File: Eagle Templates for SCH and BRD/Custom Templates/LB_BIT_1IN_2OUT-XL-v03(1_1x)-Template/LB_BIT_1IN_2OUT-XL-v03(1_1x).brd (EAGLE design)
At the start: 21.6 x 38 mm, 21 parts, among them U1 LV321SOT23-5, U2 LV321SOT23-5, U3 LV321SOT23-5

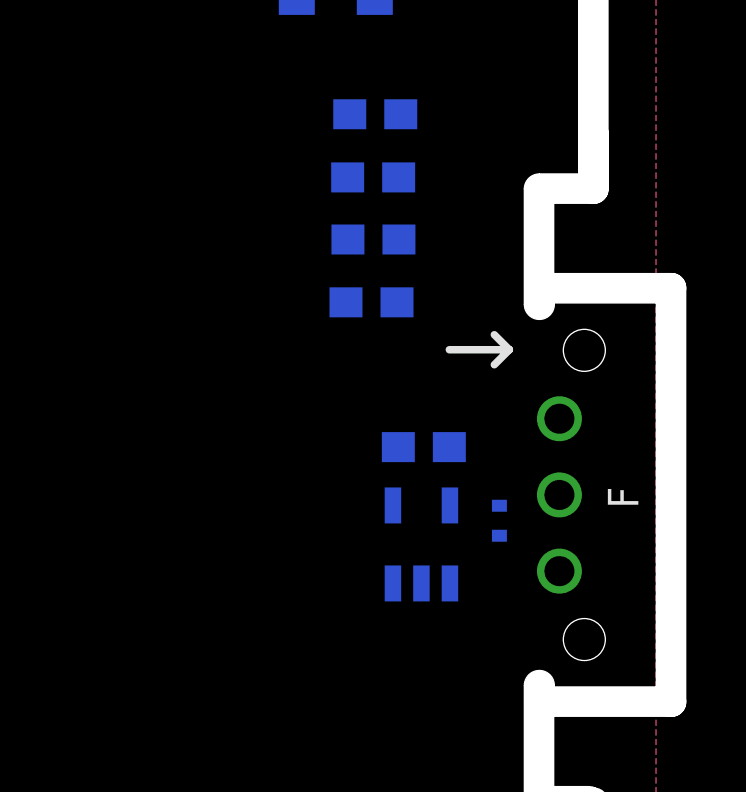
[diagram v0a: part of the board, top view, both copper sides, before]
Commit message: added bitlab logo and made minor changes to board templates. Updated littlebits library.
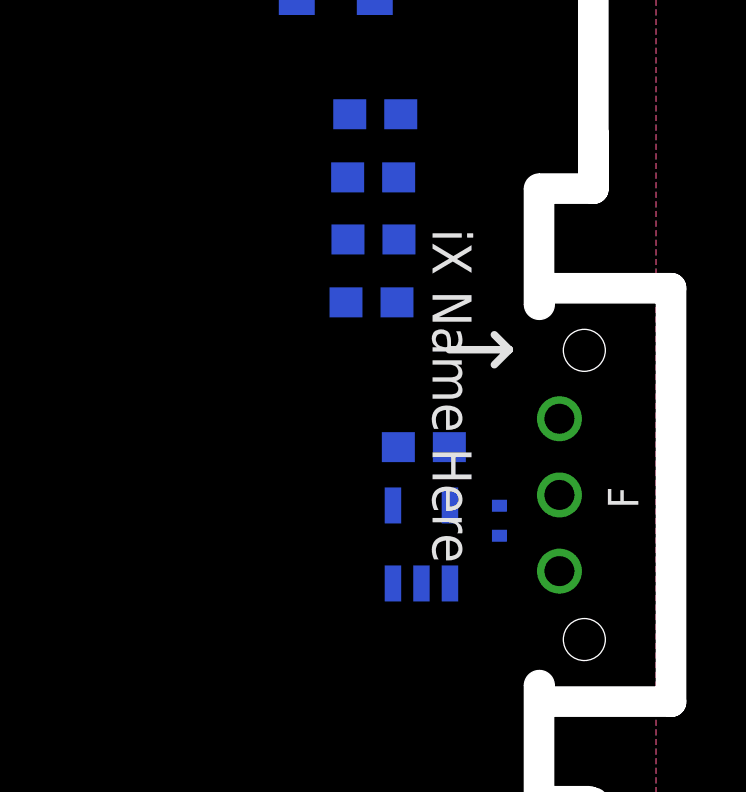
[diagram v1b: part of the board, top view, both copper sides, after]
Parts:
- added U$3: (no value), LITTLEBITS:BITLAB-LOGO
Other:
- board text added: "iX Name Here"
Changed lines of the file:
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@@
 <layer number="113" name="extra" color="10" fill="1" visible="yes" active="yes"/>
 <layer number="116" name="Patch_BOT" color="9" fill="4" visible="yes" active="yes"/>
+<layer number="118" name="Rect_Pads" color="7" fill="1" visible="no" active="yes"/>
 <layer number="121" name="_tsilk" color="7" fill="1" visible="yes" active="yes"/>
 <layer number="122" name="_bsilk" color="7" fill="1" visible="yes" active="yes"/>
@@
 <wire x1="23.625" y1="4.61" x2="23.41" y2="4.61" width="0" layer="20"/>
 <text x="4.7" y="8.2" size="0.8128" layer="16" font="vector" ratio="12" rot="MR270">revX</text>
+<text x="19.4" y="23.1175" size="1.3" layer="21" font="vector" rot="SR270" align="center">iX Name Here</text>
 </plain>
 <attributes>
@@
 <element name="U$2" library="LITTLEBITS" package="OSHWCREDIT" value="OSHWCREDIT" x="-86.995" y="-58.54"/>
 <element name="FRAME1" library="LITTLEBITS" package="FABDWG01-OHW" value="FRAME-LETTER" x="0" y="0"/>
+<element name="U$3" library="LITTLEBITS" package="BITLAB-LOGO" value="" x="18" y="27.7" rot="R270"/>
 </elements>
 <signals>

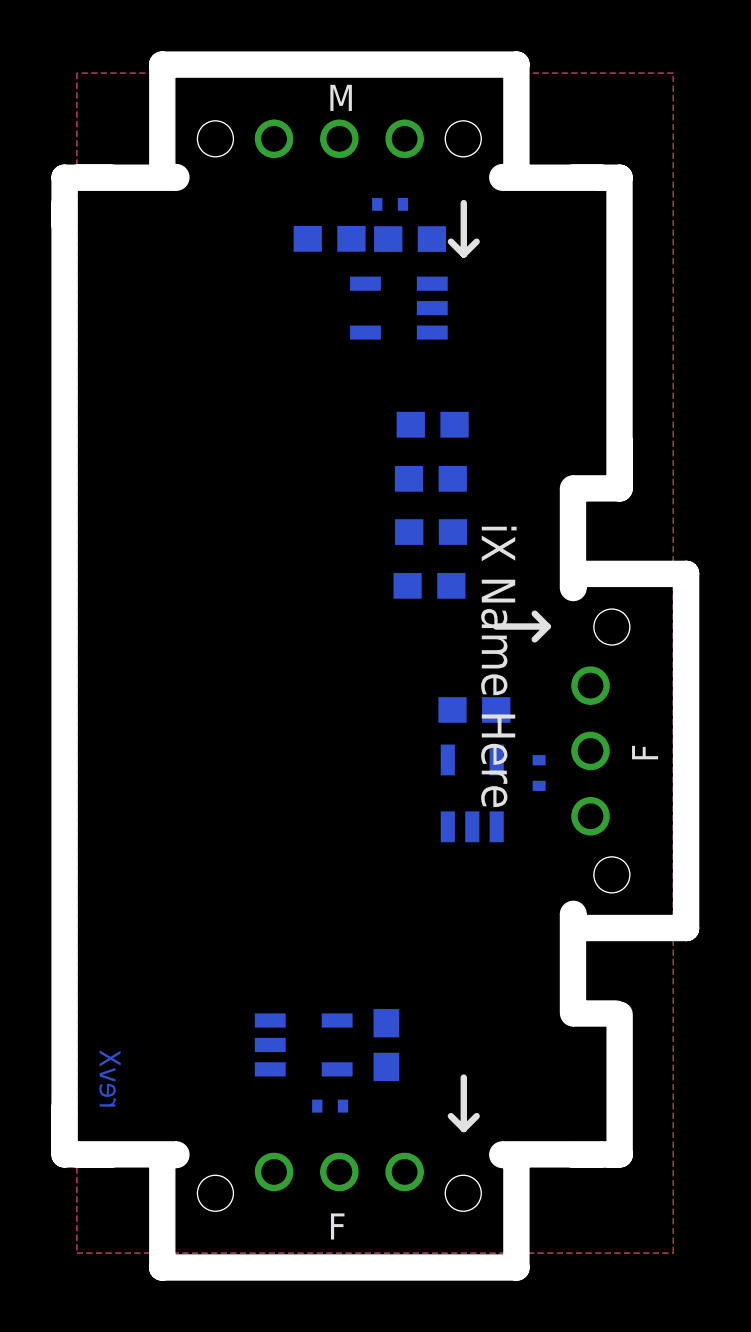
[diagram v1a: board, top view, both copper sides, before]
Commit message: Updated templates
- Added ferrite beads
- Moved text and annotations off of Nets layer
- Minor layout changes
- Removed I/O/W prefix from reference designators
- Removed output stage components from output bits
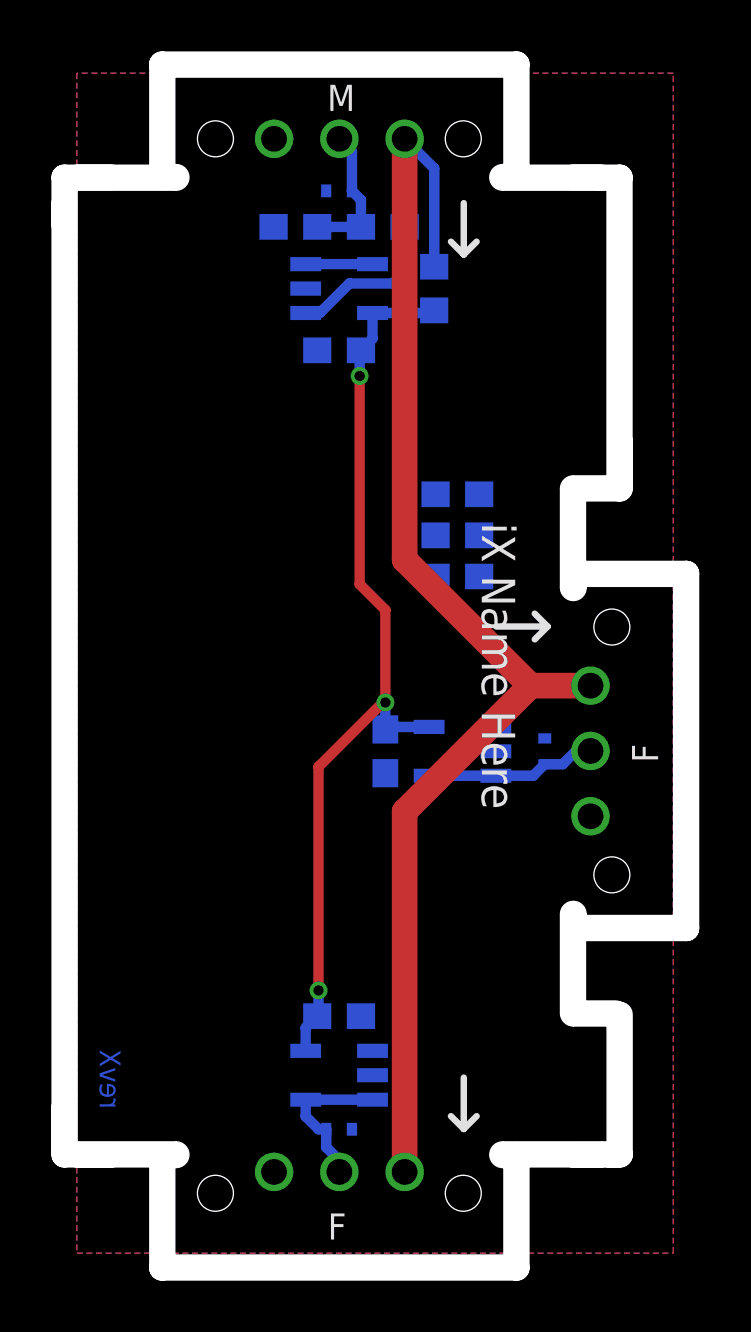
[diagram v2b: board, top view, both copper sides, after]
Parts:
- removed I?C1: 0.1uF, LITTLEBITS:CAP-0603
- removed I?C2: 10uF, LITTLEBITS:CAP-0603
- removed I?C3, I?C4: 1.0uF, LITTLEBITS:CAP-0603
- removed I?R3, I?R4: 3K3, LITTLEBITS:RES-0603
- removed I?R5: 1meg, LITTLEBITS:RES-0603
- removed I?R6: 10K, LITTLEBITS:RES-0603
- removed I?TVS1, I?TVS2, I?TVS3: ESD9B5.0ST5G, LITTLEBITS:SOD-923
- added C1: 0.1uF, LITTLEBITS:CAP-0603
- added C2: 10uF, LITTLEBITS:CAP-0603
- added C3, C4: 1.0uF, LITTLEBITS:CAP-0603
- added FB1: FERRITE-BEAD0603, LITTLEBITS:R0603
- added R3, R4: 3K3, LITTLEBITS:RES-0603
- added R5: 1meg, LITTLEBITS:RES-0603
- added R6: 10K, LITTLEBITS:RES-0603
- added TVS1, TVS2, TVS3: ESD9B5.0ST5G, LITTLEBITS:SOD-923
- moved U3 2.45 mm to (13.2, 37.8), turned to 90 degrees
- moved U2 1.81 mm to (13.2, 7.20), turned to 270 degrees
- moved U1 1.68 mm to (18.0, 19.8), turned to 270 degrees
- renumbered I32BSF1 to BSF1, I32BSF2 to BSF2, I32BSM1 to BSM1
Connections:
- new net LB_VCC: BSF1.VCC, BSF2.VCC, BSM1.VCC1, FB1.2
- net GND: now also C1.2, C2.2, C3.1, C4.1, R4.1, R5.1, TVS1.1, TVS2.1, TVS3.1; no longer I?C1.2, I?C2.2, I?C3.1, I?C4.1, I?R4.1, I?R5.1, I?TVS1.1, I?TVS2.1, I?TVS3.1
- net N$5: now also R6.1; no longer I?R6.1
- net SIG1_OUT: now also BSF1.SIG, TVS2.2; no longer I?TVS2.2
- net SIG2_OUT: now also BSF2.SIG, TVS1.2; no longer I?TVS1.2
- net SIG_IN: now also R5.2, R6.2, TVS3.2; no longer BSF1.SIG, BSF2.SIG, I?R5.2, I?R6.2, I?TVS3.2
- net VCC: now also C1.1, C3.2, C4.2, FB1.1, R3.2; no longer BSF1.VCC, BSF2.VCC, BSM1.VCC1, I?C1.1, I?C3.2, I?C4.2, I?R3.2
- net VREF: now also C2.1, R3.1, R4.2; no longer I?C2.1, I?R3.1, I?R4.2
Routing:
- net LB_VCC: track 0.00 -> 52.0 mm
- net VCC: track 0.00 -> 35.9 mm, vias 0 -> 3
- net SIG2_OUT: track 0.00 -> 6.68 mm
- net N$5: track 0.00 -> 6.26 mm
- net SIG1_OUT: track 0.00 -> 6.13 mm
- net SIG_IN: track 0.00 -> 5.47 mm
- net N$1: track 0.00 -> 2.60 mm
